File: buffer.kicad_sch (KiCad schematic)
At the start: 7 parts, among them U1 AD8066

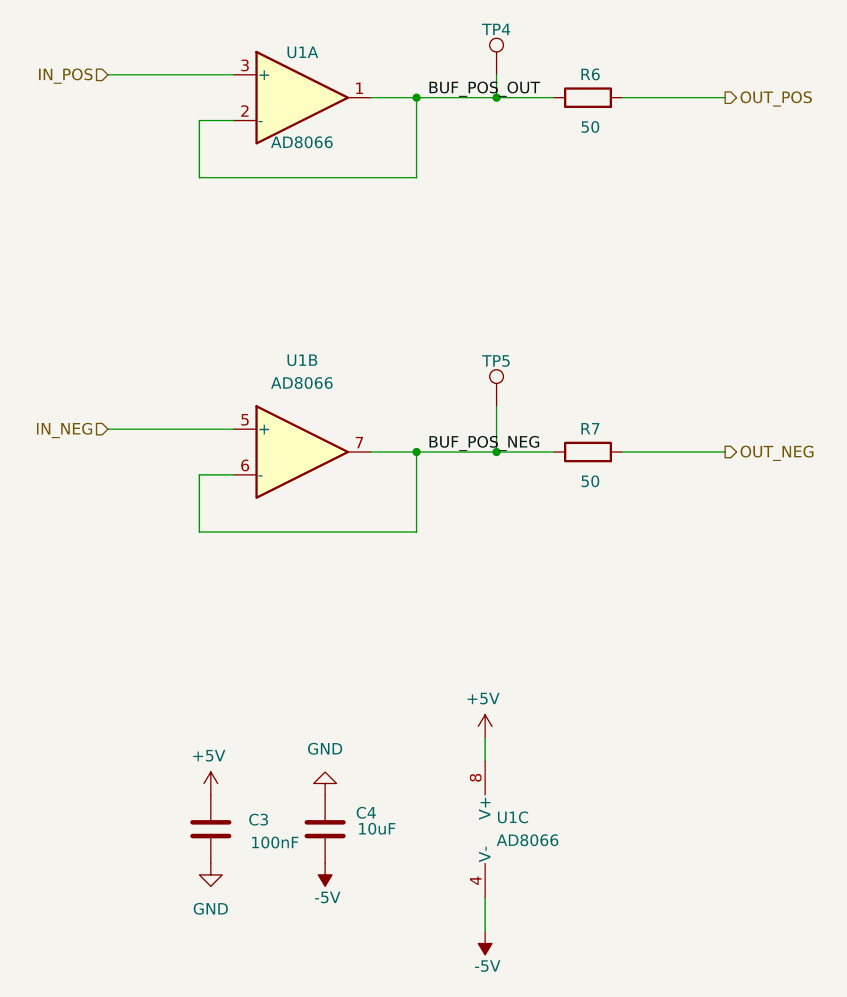
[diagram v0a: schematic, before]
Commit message: DRC completed. Need to add some 3D models.
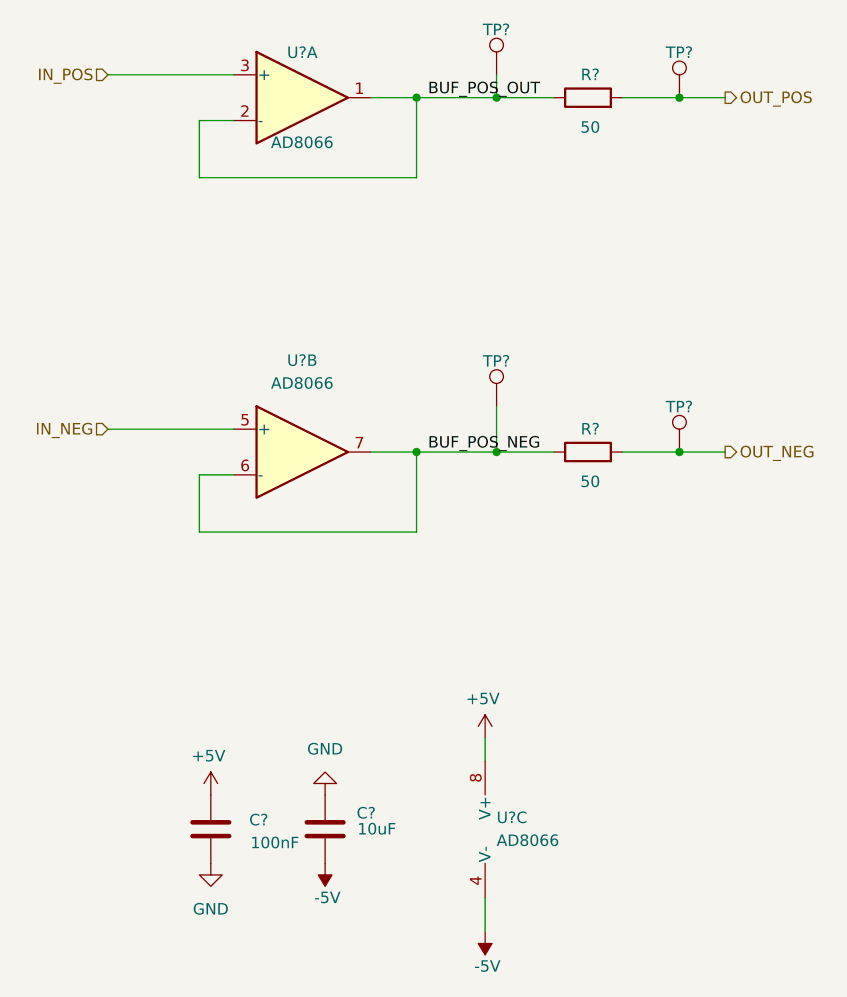
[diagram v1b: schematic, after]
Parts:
- added TP? (x2): TP, TestPoint:TestPoint_Pad_D2.0mm, symbol Connector:TestPoint
- added U? (x2): AD8066, Package_SO:SOIC-8_3.9x4.9mm_P1.27mm, symbol Amplifier_Operational:LM2904
- renumbered C4 to C?, C3 to C?, R7 to R?, R6 to R?, TP4 to TP?, TP5 to TP?, U1 to U?
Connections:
- net +5V: now also U?.8 (V+); no longer U?.8 (V+)
- net -5V: now also U?.4 (V-); no longer U?.4 (V-)
- net BUF_POS_NEG: now also U?.6 (-), U?.7; no longer U?.6 (-), U?.7
- net IN_NEG: now also U?.5 (+); no longer U?.5 (+)
- net OUT_NEG: now also TP?.1
- net OUT_POS: now also TP?.1
